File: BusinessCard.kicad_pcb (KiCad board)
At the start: 2 copper layers, 88.9 x 50.8 mm, 59 parts, among them J1 RST, J2 USB_B_Micro, SW1 SW_Push, SW10 SW_Push, SW11 SW_Push, SW12 SW_Push, SW13 SW_Push, SW14 SW_Push, SW15 SW_Push, SW16 SW_Push, SW2 SW_Push, SW3 SW_Push, SW4 SW_Push, SW5 SW_Push, SW6 SW_Push, SW7 SW_Push, SW8 SW_Push, SW9 SW_Push, U2 USBLC6-2SC6, U3 ATmega32U4-M, Y1 X322516MLB4SI

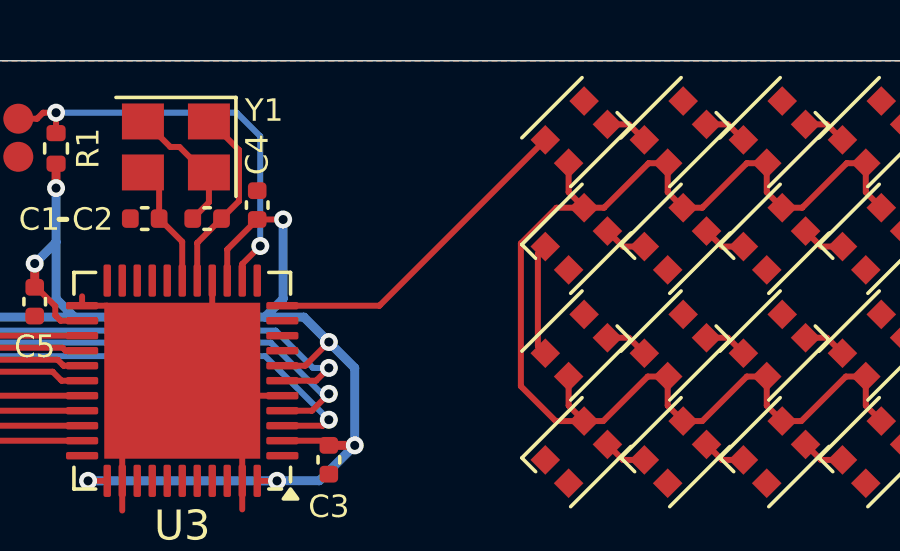
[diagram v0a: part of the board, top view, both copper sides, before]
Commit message: Add QR code with wiki link
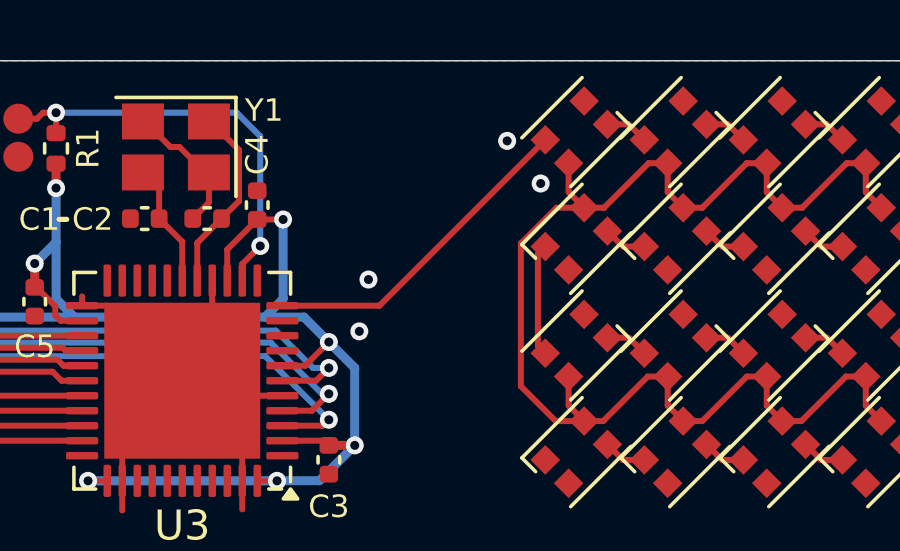
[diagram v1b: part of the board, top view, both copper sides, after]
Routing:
- net GND: vias 0 -> 4
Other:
- board text added: "Scan the QR code on the back of the card for more info."
- board text removed: "Scan the QR code above for more info."
